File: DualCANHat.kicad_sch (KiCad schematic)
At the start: 6 parts, among them J1 GPIO, U1 CAT24C256

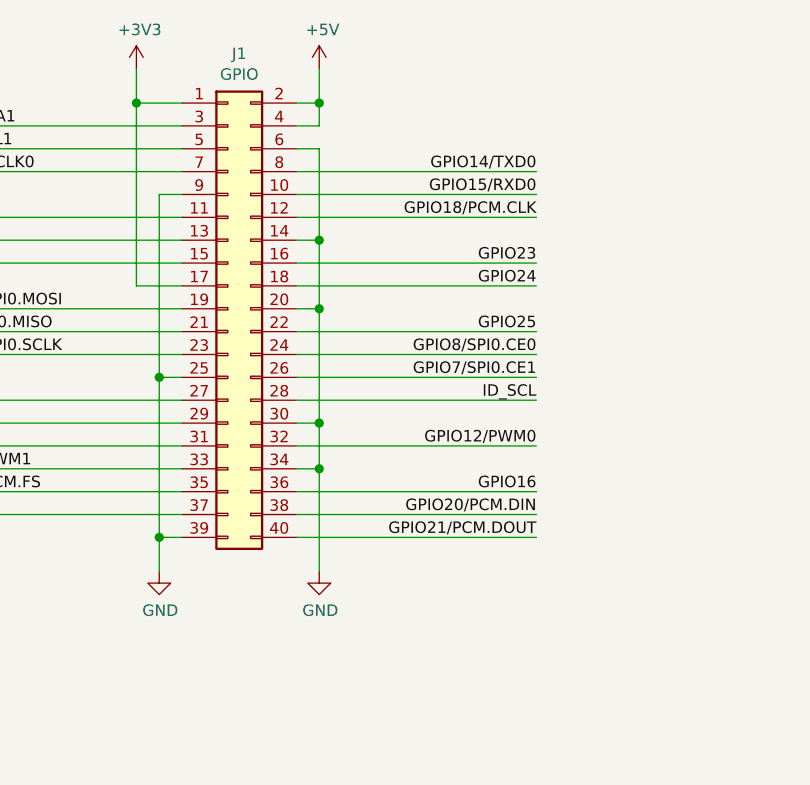
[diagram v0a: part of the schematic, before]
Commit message: Added Libraries folder and changed header to Adafruit 2223
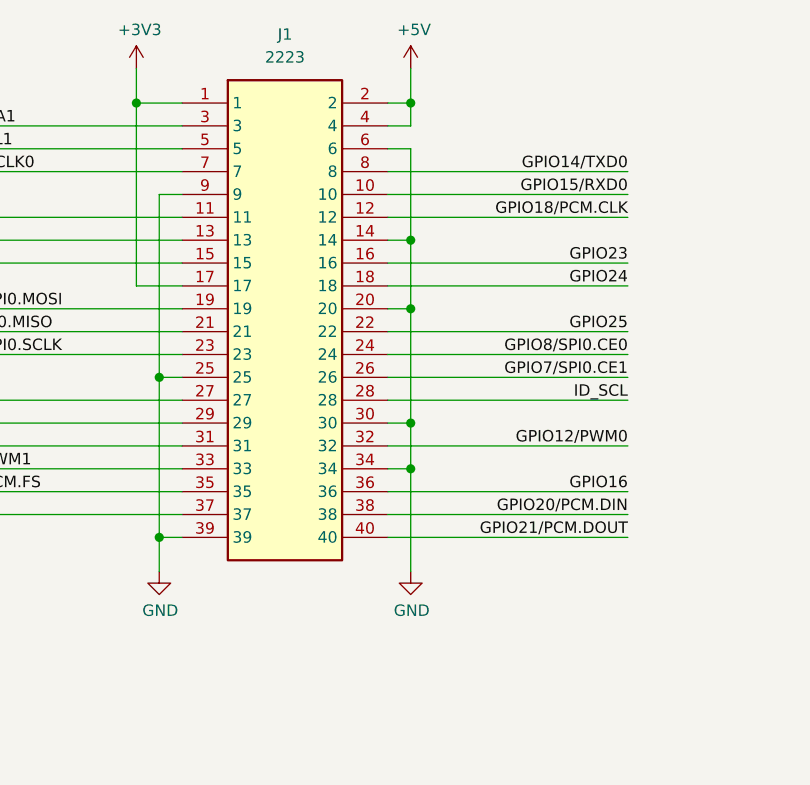
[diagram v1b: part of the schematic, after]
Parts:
- removed J1: GPIO, Connector_PinSocket_2.54mm:PinSocket_2x20_P2.54mm_Vertical, symbol Connector_Generic:Conn_02x20_Odd_Even
- added J1: 2223, RHDR40W64P254X254_2X20_5105X500X865P, symbol Adafruit:2223
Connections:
- net +3V3: now also J1.1, J1.17
- net +5V: now also J1.2, J1.4
- net GND: now also J1.14, J1.20, J1.25, J1.30, J1.34, J1.39, J1.6, J1.9
- net GPIO10/SPI0.MOSI: now also J1.19
- net GPIO11/SPI0.SCLK: now also J1.23
- net GPIO12/PWM0: now also J1.32
- net GPIO13/PWM1: now also J1.33
- net GPIO14/TXD0: now also J1.8
- net GPIO15/RXD0: now also J1.10
- net GPIO16: now also J1.36
- net GPIO17: now also J1.11
- net GPIO18/PCM.CLK: now also J1.12
- net GPIO19/PCM.FS: now also J1.35
- net GPIO20/PCM.DIN: now also J1.38
- net GPIO21/PCM.DOUT: now also J1.40
- net GPIO22: now also J1.15
- net GPIO23: now also J1.16
- net GPIO24: now also J1.18
- net GPIO25: now also J1.22
- net GPIO26: now also J1.37
- net GPIO27: now also J1.13
- net GPIO2/SDA1: now also J1.3
- net GPIO3/SCL1: now also J1.5
- net GPIO4/GPCLK0: now also J1.7
- net GPIO5: now also J1.29
- net GPIO6: now also J1.31
- net GPIO7/SPI0.CE1: now also J1.26
- net GPIO8/SPI0.CE0: now also J1.24
- net GPIO9/SPI0.MISO: now also J1.21
- net ID_SCL: now also J1.28
- net ID_SDA: now also J1.27

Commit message: Added more datasheets, symbols, and footprints
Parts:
- added U2, U3: PTCAN1044ADDFRQ1, DDF0008A-IPC_A, symbol Texas Instruments:PTCAN1044ADDFRQ1
- added U4, U5: MCP2518FDT-E/QBB, VDFN14_QBB_MCH, symbol Microchip:MCP2518FDT-E_QBB

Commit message: Placed parts in schematic
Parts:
- removed U2, U3: PTCAN1044ADDFRQ1, DDF0008A-IPC_A, symbol Texas Instruments:PTCAN1044ADDFRQ1
- added U2, U3: TCAN1044ADDFRQ1, DDF0008A-IPC_A, symbol Texas Instruments:TCAN1044ADDFRQ1
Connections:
- net +3V3: no longer J1.1, J1.17
- net GND: now also U4.15 (EP), U4.7 (VSS), U5.15 (EP), U5.7 (VSS), U2.2 (GND), U2.8 (STB), U3.2 (GND), U3.8 (STB)
- net at U5.1 (TXCAN): now also U3.1 (TXD)
- net P3V3: now reaches U5.14 (VDD)
- net P3V3: now also J1.1, J1.17, U4.14 (VDD), U2.5 (VIO), U3.5 (VIO)
- net at U5.2 (RXCAN): now also U3.4 (RXD)
- net at U4.1 (TXCAN): now also U2.1 (TXD)
- net at U4.2 (RXCAN): now also U2.4 (RXD)
- net +5V renamed P5V
- net P5V: now also U2.3 (VCC), U3.3 (VCC)
